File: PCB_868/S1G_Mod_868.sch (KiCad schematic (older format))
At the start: 18 parts

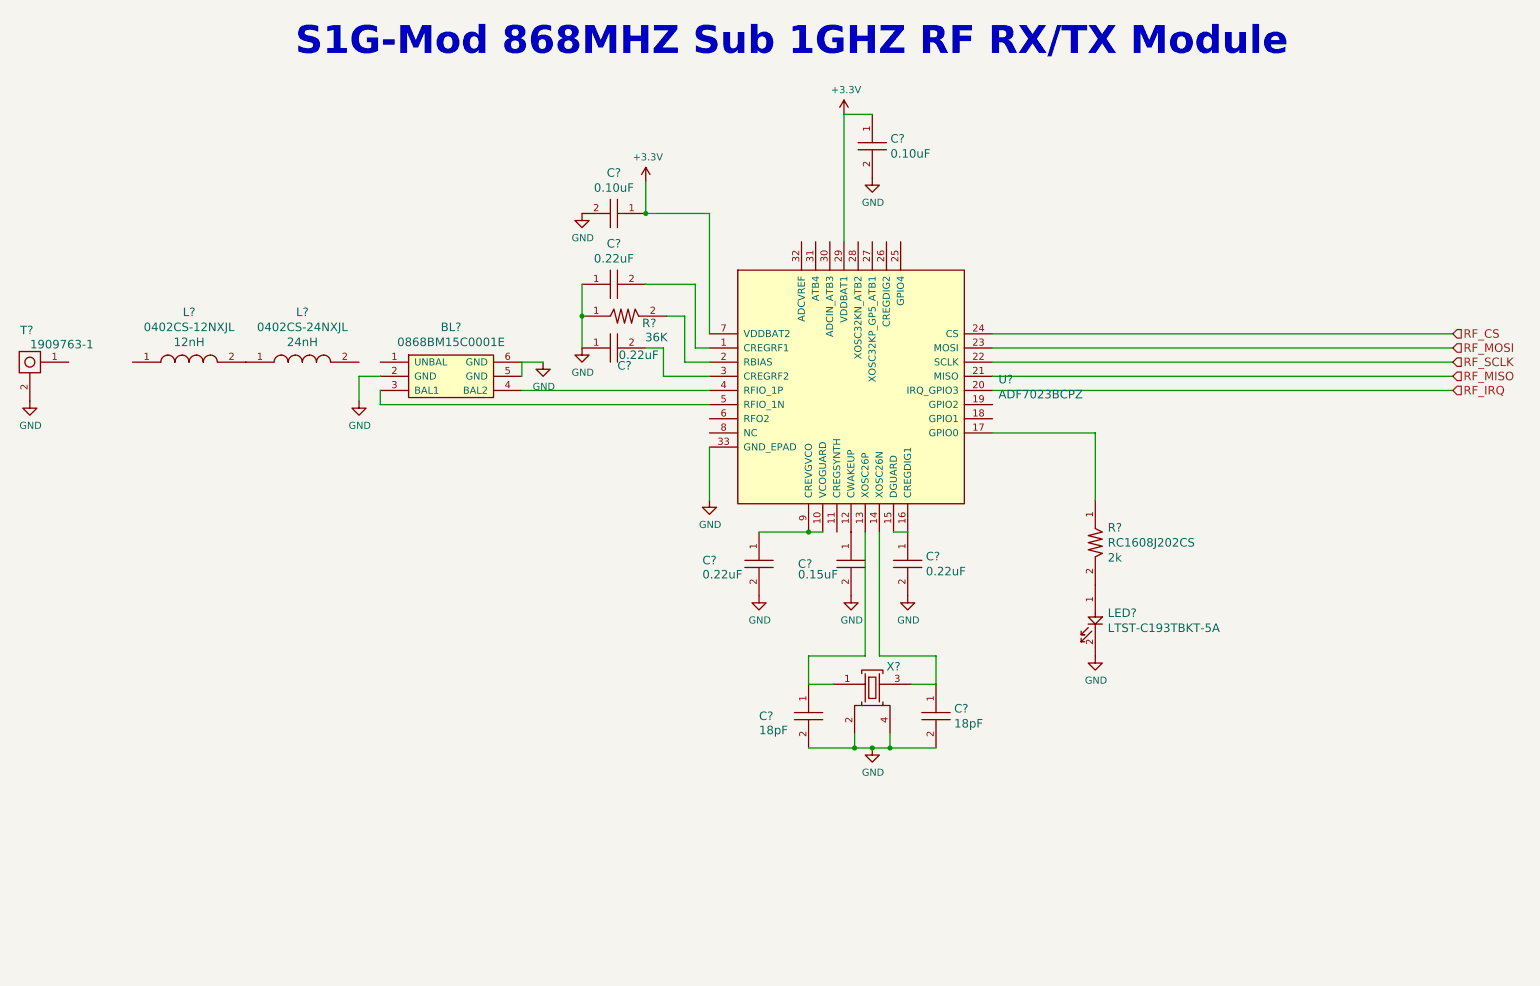
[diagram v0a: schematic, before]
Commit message: 868MHZ
Significant progress made with 868MHZ schematic, near complete just
researching the output section more before commiting to component and
circuit choices.
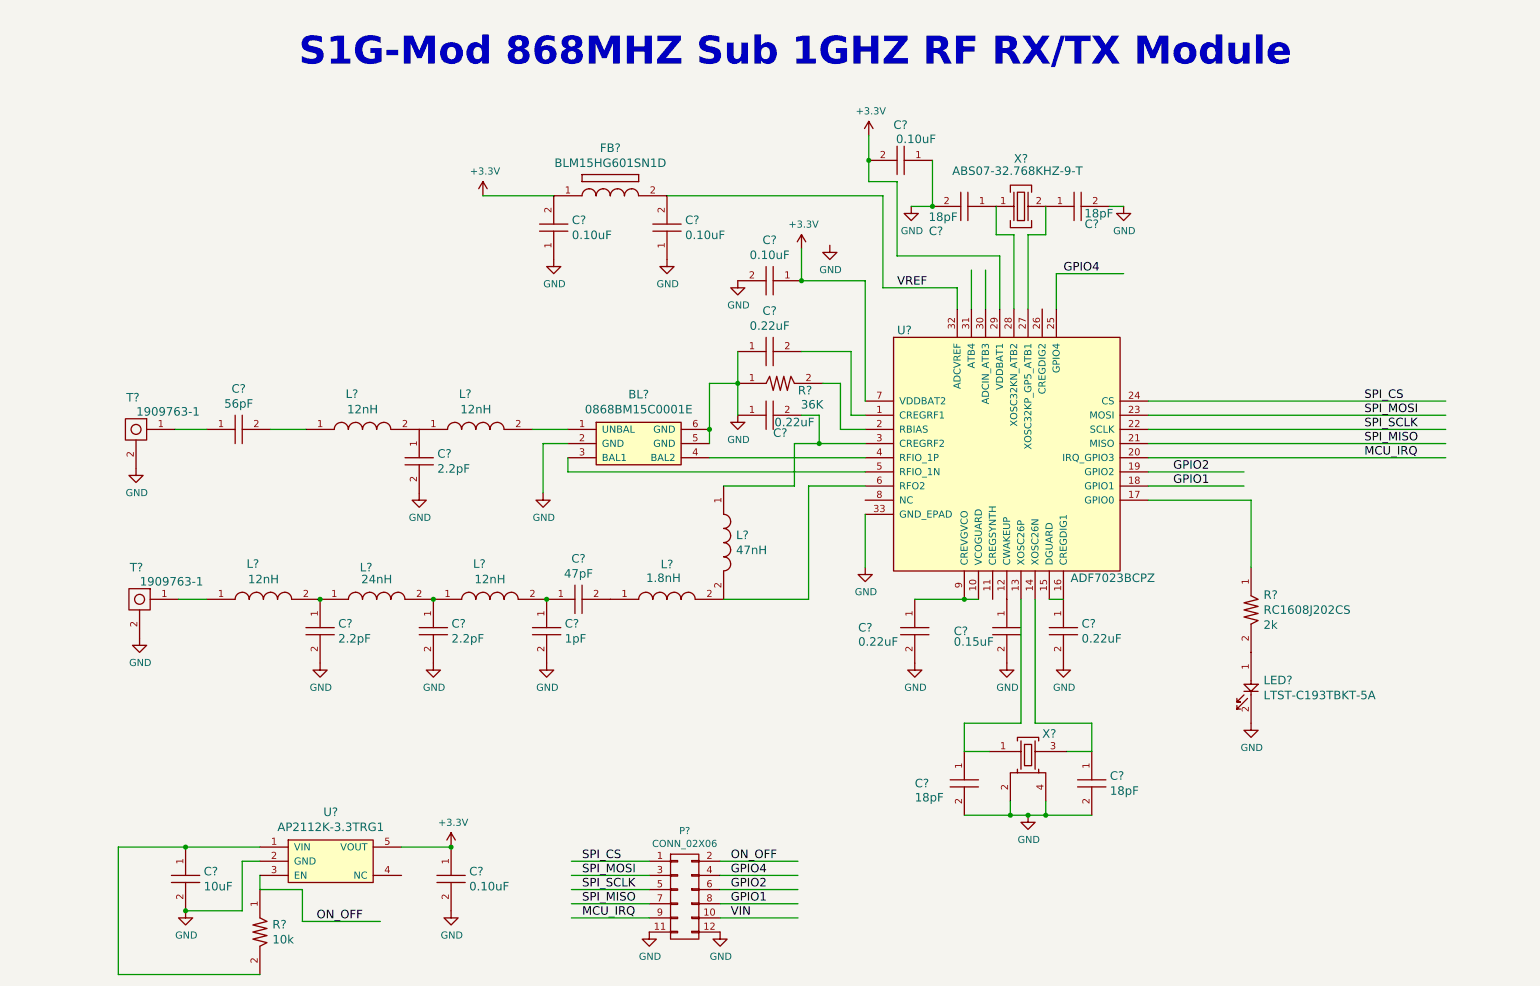
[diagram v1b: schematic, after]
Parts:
- removed BL?: 0868BM15C0001E, PCB_Footprints:0868BM15C0001E, symbol 0868BM15C0001E
- added BL?: 0868BM15C0001E, PCB_Footprints:0868BM15C0001E, symbol 0868BM15C0001E
- added C? (x3): CL05B104JP5NNNC, PCB_Footprints:C0402, symbol CL05B104JP5NNNC
- added C?: CL10A106KQ8NNNC, PCB_Footprints:C0603, symbol CL10A106KQ8NNNC
- added C? (x2): CL05C180GB5NCNC, PCB_Footprints:C0402, symbol CL05C180GB5NCNC
- added C?: CBR04C470F3GAC, PCB_Footprints:C0402, symbol CBR04C470F3GAC
- added C? (x3): GJM1555C1H2R2WB01D, PCB_Footprints:C0402, symbol GJM1555C1H2R2WB01D
- added C?: GJM1555C1H1R0BB01D, PCB_Footprints:C0402, symbol GJM1555C1H1R0BB01D
- added C?: CBR04C560F1GAC, PCB_Footprints:C0402, symbol CBR04C560F1GAC
- added FB?: BLM15HG601SN1D, PCB_Footprints:BLM15HG601SN1D, symbol BLM15HG601SN1D
- added L?: 0402CS-47NXJL, PCB_Footprints:L0402, symbol 0402CS-47NXJL
- added L?: 0402CS-1N8XJL, PCB_Footprints:L0402, symbol 0402CS-1N8XJL
- added L? (x3): 0402CS-12NXJL, PCB_Footprints:L0402, symbol 0402CS-12NXJL
- added P?: CONN_02X06, symbol CONN_02X06
- added R?: RC1005F103CS, PCB_Footprints:R0402, symbol RC1005F103CS
- added T?: 1909763-1, PCB_Footprints:1909763-1, symbol 1909763-1
- added U?: AP2112K-3.3TRG1, PCB_Footprints:AP2112K-3.3TRG1, symbol AP2112K-3.3TRG1
- added X?: ABS07-32.768KHZ-9-T, PCB_Footprints:ABS07-32.768KHZ-9-T, symbol ABS07-32.768KHZ-9-T
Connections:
- net labels added: GPIO1, GPIO2, GPIO4, MCU_IRQ, ON_OFF, SPI_CS, SPI_MISO, SPI_MOSI, SPI_SCLK, VIN, VREF
- net labels removed: RF_CS, RF_IRQ, RF_MISO, RF_MOSI, RF_SCLK
- wire segments 43 -> 96
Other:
- moved on the sheet: C?, L?, LED?, R?, T?, U?, X?

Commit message: PCB Created
PCB created and placemetn started. Going to be a more robust
implementatinn of XBee pro but bigger formfactor. going to require dual
antennas or external mixrer (perhaps another PCB "? )
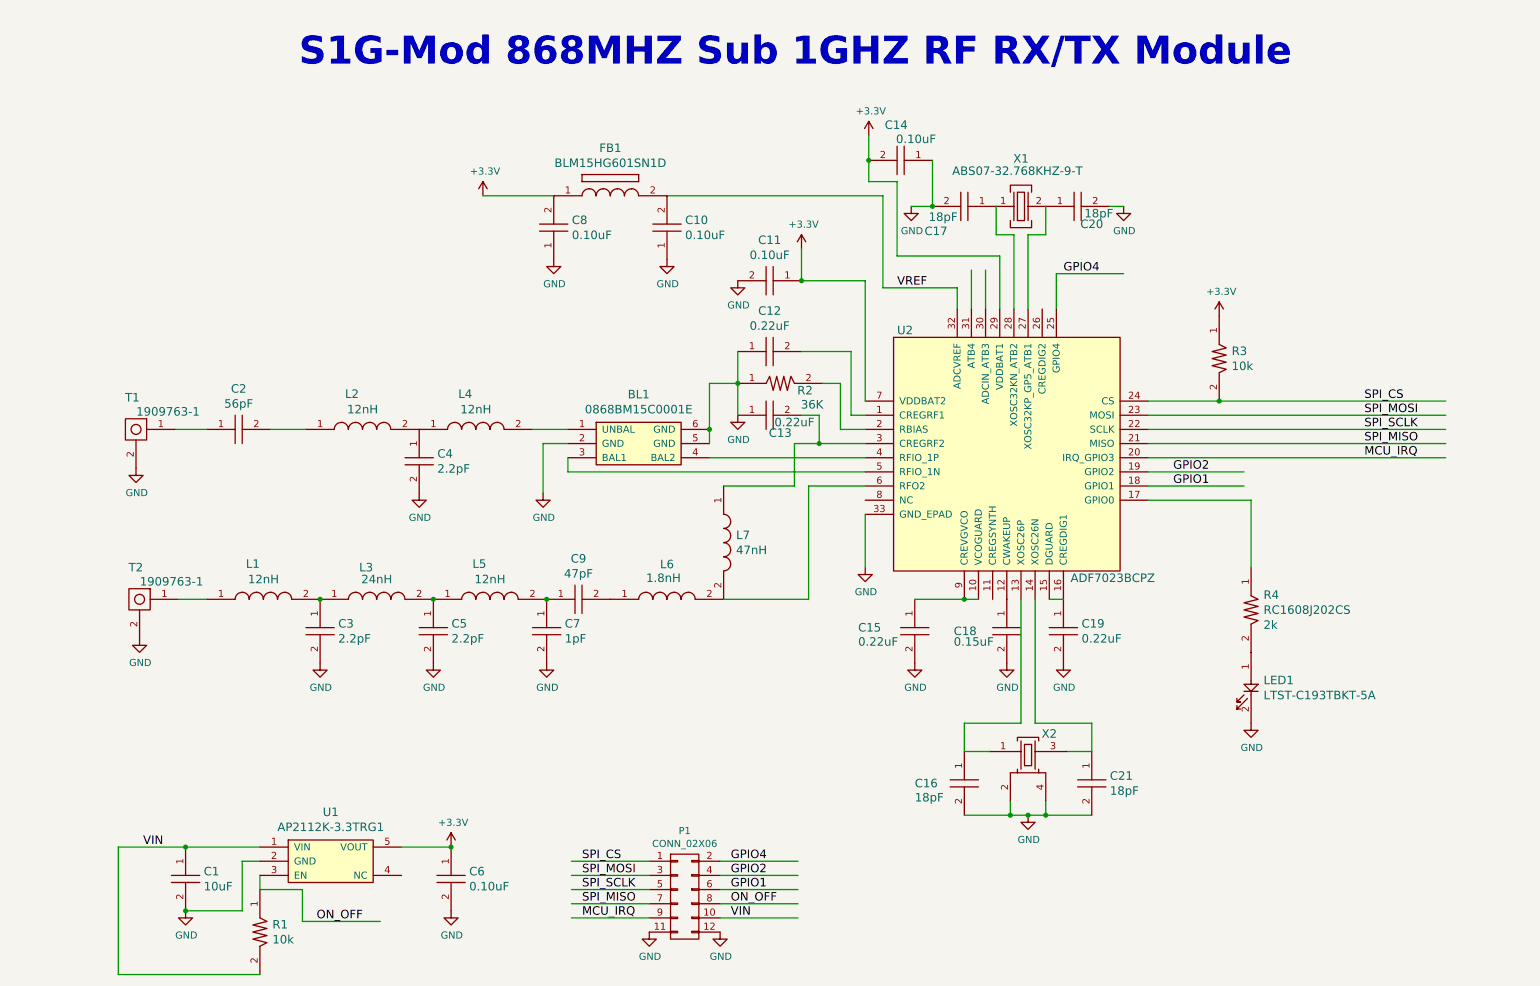
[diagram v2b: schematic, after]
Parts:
- added R3: RC1005F103CS, PCB_Footprints:R0402, symbol RC1005F103CS
- P1: renamed from P?; footprint (none) -> Pin_Headers:Pin_Header_Angled_2x06
- gave numbers to parts that had none: 40
